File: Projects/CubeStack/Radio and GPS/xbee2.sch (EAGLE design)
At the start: 78 parts, among them Q1 310mA/60V/1.6Ω, Q2 310mA/60V/1.6Ω, Q3 310mA/60V/1.6Ω, Q4 310mA/60V/1.6Ω, U1 TS3USB221A, U2 SPARKFUN-IC-POWER_V_REG_MIC52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, U3 TS3USB221A, U4 SPARKFUN-IC-POWER_V_REG_MIC52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, U5 Value, U6 CPSS_IC_TPS62130_RGT_16

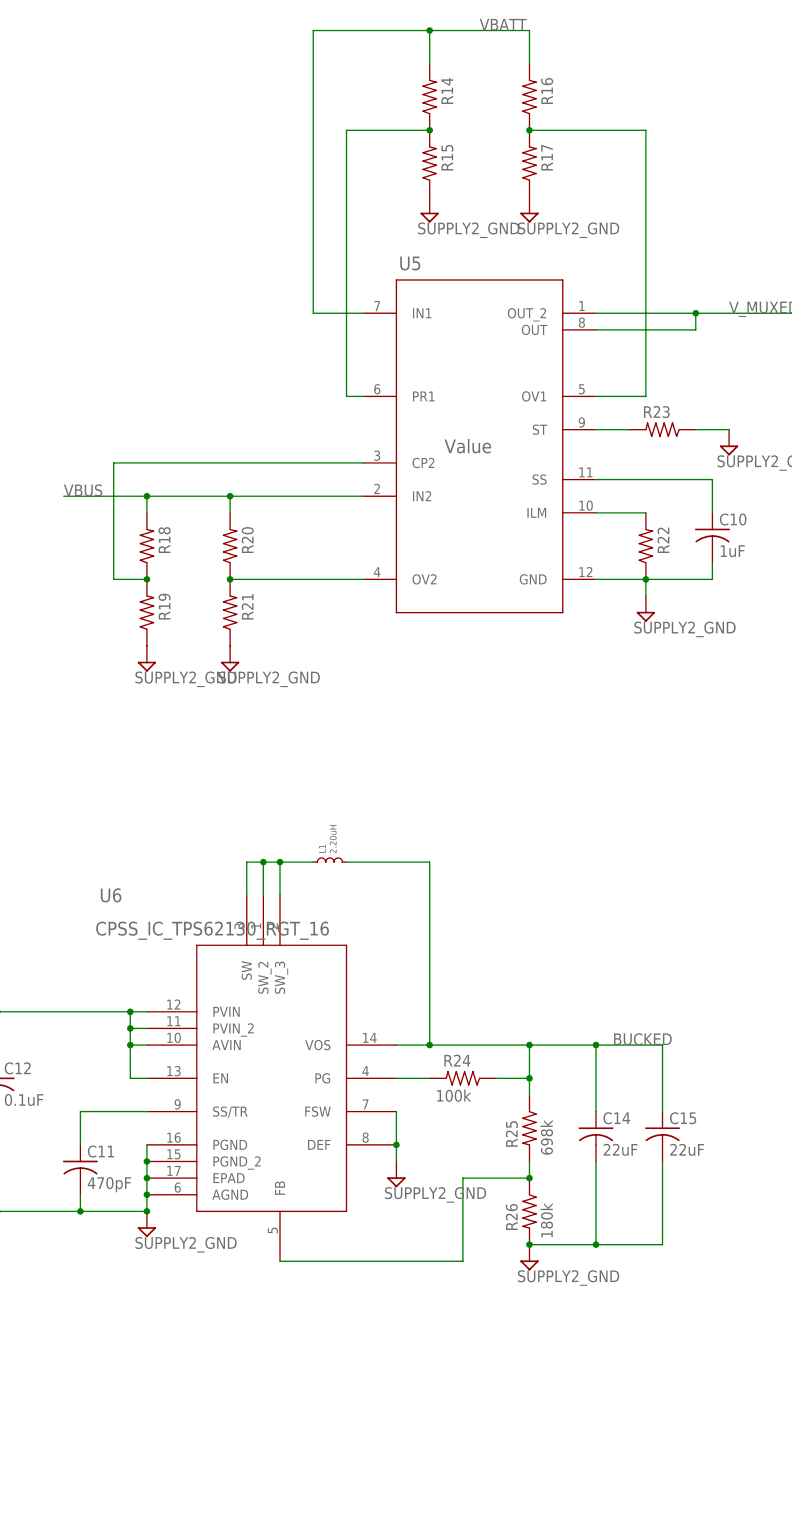
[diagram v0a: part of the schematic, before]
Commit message: Added some part values
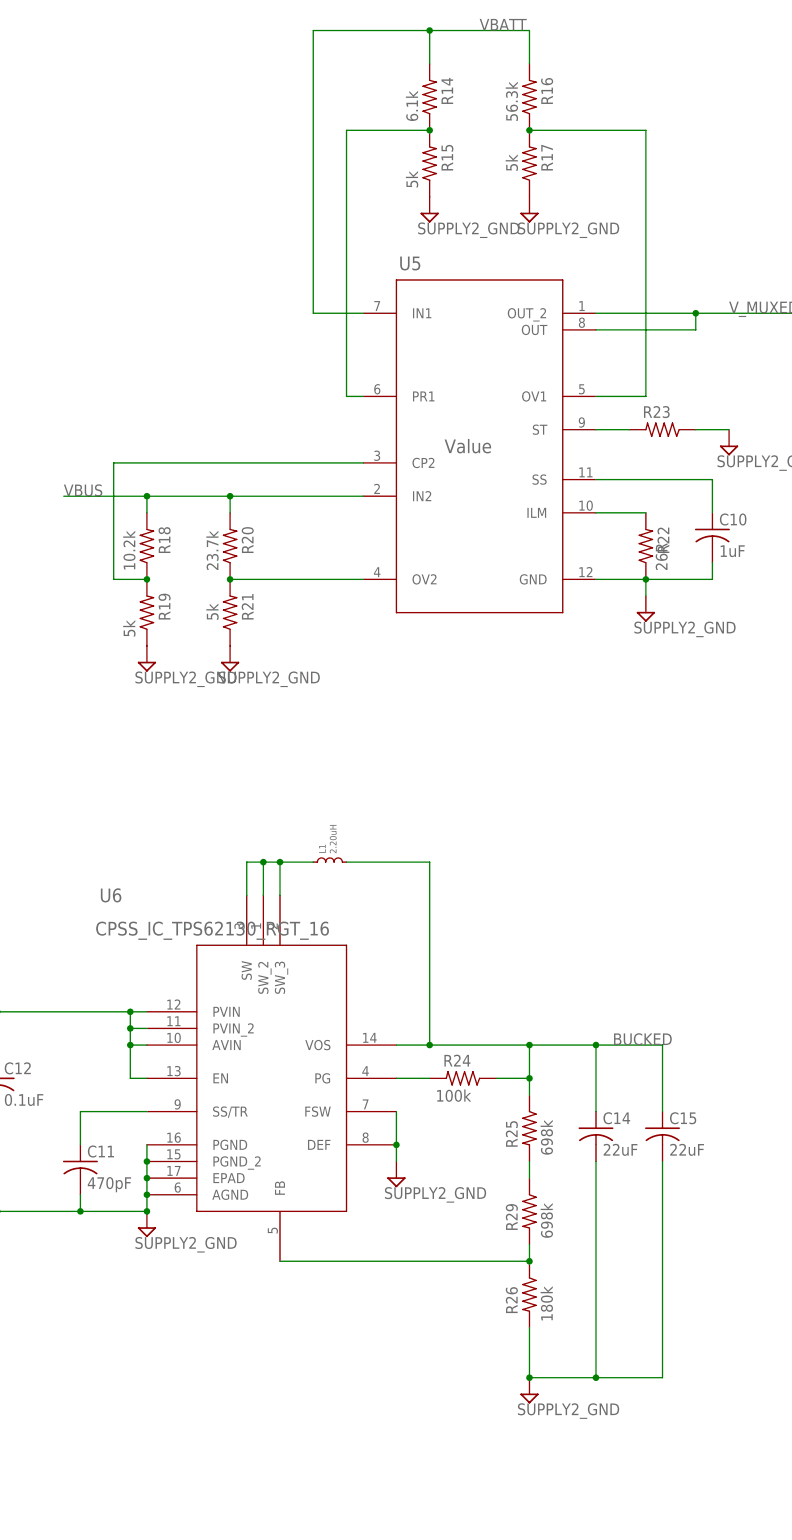
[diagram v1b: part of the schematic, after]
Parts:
- added R29: 698k, xbee2:RESISTOR_R-US_R0402
- R14: value (none) -> 6.1k
- R15, R17, R19, R21: value (none) -> 5k
- R16: value (none) -> 56.3k
- R18: value (none) -> 10.2k
- R20: value (none) -> 23.7k
- R22: value (none) -> 26R
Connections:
- new net N$40: R25.2, R29.1
- net N$24: now also R29.2; no longer R25.2
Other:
- moved on the sheet: R26
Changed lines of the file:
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@@
 <drawing>
 <settings>
-<setting alwaysvectorfont="no"/>
+<setting alwaysvectorfont="yes"/>
 <setting verticaltext="up"/>
 </settings>
@@
 <part name="R13" library="xbee2" deviceset="RESISTOR_R-US_" device="R0402" value="10k"/>
 <part name="U5" library="xbee2" deviceset="CPSS_IC_TPS2121RUXR" device="" value="Value"/>
-<part name="R14" library="xbee2" deviceset="RESISTOR_R-US_" device="R0402"/>
-<part name="R15" library="xbee2" deviceset="RESISTOR_R-US_" device="R0402"/>
+<part name="R14" library="xbee2" deviceset="RESISTOR_R-US_" device="R0402" value="6.1k"/>
+<part name="R15" library="xbee2" deviceset="RESISTOR_R-US_" device="R0402" value="5k"/>
 <part name="SUPPLY12" library="xbee2" deviceset="SUPPLY2_GND" device=""/>
-<part name="R16" library="xbee2" deviceset="RESISTOR_R-US_" device="R0402"/>
-<part name="R17" library="xbee2" deviceset="RESISTOR_R-US_" device="R0402"/>
+<part name="R16" library="xbee2" deviceset="RESISTOR_R-US_" device="R0402" value="56.3k"/>
+<part name="R17" library="xbee2" deviceset="RESISTOR_R-US_" device="R0402" value="5k"/>
 <part name="SUPPLY13" library="xbee2" deviceset="SUPPLY2_GND" device=""/>
-<part name="R18" library="xbee2" deviceset="RESISTOR_R-US_" device="R0402"/>
-<part name="R19" library="xbee2" deviceset="RESISTOR_R-US_" device="R0402"/>
+<part name="R18" library="xbee2" deviceset="RESISTOR_R-US_" device="R0402" value="10.2k"/>
+<part name="R19" library="xbee2" deviceset="RESISTOR_R-US_" device="R0402" value="5k"/>
 <part name="SUPPLY14" library="xbee2" deviceset="SUPPLY2_GND" device=""/>
-<part name="R20" library="xbee2" deviceset="RESISTOR_R-US_" device="R0402"/>
-<part name="R21" library="xbee2" deviceset="RESISTOR_R-US_" device="R0402"/>
+<part name="R20" library="xbee2" deviceset="RESISTOR_R-US_" device="R0402" value="23.7k"/>
+<part name="R21" library="xbee2" deviceset="RESISTOR_R-US_" device="R0402" value="5k"/>
 <part name="SUPPLY15" library="xbee2" deviceset="SUPPLY2_GND" device=""/>
-<part name="R22" library="xbee2" deviceset="RESISTOR_R-US_" device="R0402"/>
+<part name="R22" library="xbee2" deviceset="RESISTOR_R-US_" device="R0402" value="26R"/>
 <part name="C10" library="xbee2" deviceset="RESISTOR_C-US" device="C0402" value="1uF"/>
 <part name="SUPPLY16" library="xbee2" deviceset="SUPPLY2_GND" device=""/>
@@
 <part name="SJ7" library="xbee2" deviceset="JUMPER_SJ2W" device=""/>
 <part name="SJ8" library="xbee2" deviceset="JUMPER_SJ2W" device=""/>
+<part name="R29" library="xbee2" deviceset="RESISTOR_R-US_" device="R0402" value="698k"/>
 </parts>
 <sheets>
@@
 <instance part="R14" gate="G$1" x="-60.96" y="312.42" smashed="yes" rot="R90">
 <attribute name="NAME" x="-57.3786" y="311.15" size="1.778" layer="95" rot="R90"/>
-<attribute name="VALUE" x="-57.658" y="308.61" size="1.778" layer="96" rot="R90"/>
+<attribute name="VALUE" x="-62.738" y="308.61" size="1.778" layer="96" rot="R90"/>
 </instance>
 <instance part="R15" gate="G$1" x="-60.96" y="302.26" smashed="yes" rot="R90">
 <attribute name="NAME" x="-57.3786" y="300.99" size="1.778" layer="95" rot="R90"/>
-<attribute name="VALUE" x="-57.658" y="298.45" size="1.778" layer="96" rot="R90"/>
+<attribute name="VALUE" x="-62.738" y="298.45" size="1.778" layer="96" rot="R90"/>
 </instance>
 <instance part="SUPPLY12" gate="GND" x="-60.96" y="294.64" smashed="yes">
@@
 <instance part="R16" gate="G$1" x="-45.72" y="312.42" smashed="yes" rot="R90">
 <attribute name="NAME" x="-42.1386" y="311.15" size="1.778" layer="95" rot="R90"/>
-<attribute name="VALUE" x="-42.418" y="308.61" size="1.778" layer="96" rot="R90"/>
+<attribute name="VALUE" x="-47.498" y="308.61" size="1.778" layer="96" rot="R90"/>
 </instance>
 <instance part="R17" gate="G$1" x="-45.72" y="302.26" smashed="yes" rot="R90">
 <attribute name="NAME" x="-42.1386" y="300.99" size="1.778" layer="95" rot="R90"/>
-<attribute name="VALUE" x="-42.418" y="298.45" size="1.778" layer="96" rot="R90"/>
+<attribute name="VALUE" x="-47.498" y="300.99" size="1.778" layer="96" rot="R90"/>
 </instance>
 <instance part="SUPPLY13" gate="GND" x="-45.72" y="294.64" smashed="yes">
@@
 <instance part="R18" gate="G$1" x="-104.14" y="243.84" smashed="yes" rot="R90">
 <attribute name="NAME" x="-100.5586" y="242.57" size="1.778" layer="95" rot="R90"/>
-<attribute name="VALUE" x="-100.838" y="240.03" size="1.778" layer="96" rot="R90"/>
+<attribute name="VALUE" x="-105.918" y="240.03" size="1.778" layer="96" rot="R90"/>
 </instance>
 <instance part="R19" gate="G$1" x="-104.14" y="233.68" smashed="yes" rot="R90">
 <attribute name="NAME" x="-100.5586" y="232.41" size="1.778" layer="95" rot="R90"/>
-<attribute name="VALUE" x="-100.838" y="229.87" size="1.778" layer="96" rot="R90"/>
+<attribute name="VALUE" x="-105.918" y="229.87" size="1.778" layer="96" rot="R90"/>
 </instance>
 <instance part="SUPPLY14" gate="GND" x="-104.14" y="226.06" smashed="yes">
@@
 <instance part="R20" gate="G$1" x="-91.44" y="243.84" smashed="yes" rot="R90">
 <attribute name="NAME" x="-87.8586" y="242.57" size="1.778" layer="95" rot="R90"/>
-<attribute name="VALUE" x="-88.138" y="240.03" size="1.778" layer="96" rot="R90"/>
+<attribute name="VALUE" x="-93.218" y="240.03" size="1.778" layer="96" rot="R90"/>
 </instance>
 <instance part="R21" gate="G$1" x="-91.44" y="233.68" smashed="yes" rot="R90">
 <attribute name="NAME" x="-87.8586" y="232.41" size="1.778" layer="95" rot="R90"/>
-<attribute name="VALUE" x="-88.138" y="229.87" size="1.778" layer="96" rot="R90"/>
+<attribute name="VALUE" x="-93.218" y="232.41" size="1.778" layer="96" rot="R90"/>
 </instance>
 <instance part="SUPPLY15" gate="GND" x="-91.44" y="226.06" smashed="yes">
@@
 <attribute name="VALUE" x="-43.942" y="156.21" size="1.778" layer="96" rot="R270"/>
 </instance>
-<instance part="R26" gate="G$1" x="-45.72" y="142.24" smashed="yes" rot="R270">
-<attribute name="NAME" x="-49.3014" y="143.51" size="1.778" layer="95" rot="R270"/>
-<attribute name="VALUE" x="-43.942" y="143.51" size="1.778" layer="96" rot="R270"/>
-</instance>
-<instance part="SUPPLY20" gate="GND" x="-45.72" y="134.62" smashed="yes">
-<attribute name="VALUE" x="-47.625" y="131.445" size="1.778" layer="96"/>
+<instance part="R26" gate="G$1" x="-45.72" y="129.54" smashed="yes" rot="R270">
+<attribute name="NAME" x="-49.3014" y="130.81" size="1.778" layer="95" rot="R270"/>
+<attribute name="VALUE" x="-43.942" y="130.81" size="1.778" layer="96" rot="R270"/>
+</instance>
+<instance part="SUPPLY20" gate="GND" x="-45.72" y="114.3" smashed="yes">
+<attribute name="VALUE" x="-47.625" y="111.125" size="1.778" layer="96"/>
 </instance>
 <instance part="L1" gate="G$1" x="-76.2" y="195.58" smashed="yes">
@@
 <attribute name="NAME" x="198.12" y="-63.119" size="1.778" layer="95"/>
 <attribute name="VALUE" x="198.12" y="-65.405" size="1.778" layer="96"/>
+</instance>
+<instance part="R29" gate="G$1" x="-45.72" y="142.24" smashed="yes" rot="R270">
+<attribute name="NAME" x="-49.3014" y="143.51" size="1.778" layer="95" rot="R270"/>
+<attribute name="VALUE" x="-43.942" y="143.51" size="1.778" layer="96" rot="R270"/>
 </instance>
 </instances>
@@
 <pinref part="SUPPLY20" gate="GND" pin="GND"/>
 <pinref part="C14" gate="G$1" pin="2"/>
-<wire x1="-35.56" y1="149.86" x2="-35.56" y2="137.16" width="0.1524" layer="91"/>
-<wire x1="-35.56" y1="137.16" x2="-45.72" y2="137.16" width="0.1524" layer="91"/>
-<junction x="-45.72" y="137.16"/>
+<wire x1="-35.56" y1="149.86" x2="-35.56" y2="116.84" width="0.1524" layer="91"/>
+<wire x1="-35.56" y1="116.84" x2="-45.72" y2="116.84" width="0.1524" layer="91"/>
+<junction x="-45.72" y="116.84"/>
 <pinref part="C15" gate="G$1" pin="2"/>
-<wire x1="-25.4" y1="149.86" x2="-25.4" y2="137.16" width="0.1524" layer="91"/>
-<wire x1="-25.4" y1="137.16" x2="-35.56" y2="137.16" width="0.1524" layer="91"/>
-<junction x="-35.56" y="137.16"/>
+<wire x1="-25.4" y1="149.86" x2="-25.4" y2="116.84" width="0.1524" layer="91"/>
+<wire x1="-25.4" y1="116.84" x2="-35.56" y2="116.84" width="0.1524" layer="91"/>
+<junction x="-35.56" y="116.84"/>
+<wire x1="-45.72" y1="116.84" x2="-45.72" y2="124.46" width="0.1524" layer="91"/>
 </segment>
 <segment>
@@
 <net name="N$24" class="0">
 <segment>
-<pinref part="R25" gate="G$1" pin="2"/>
 <pinref part="R26" gate="G$1" pin="1"/>
-<wire x1="-45.72" y1="149.86" x2="-45.72" y2="147.32" width="0.1524" layer="91"/>
 <pinref part="U6" gate="A" pin="FB"/>
-<wire x1="-83.82" y1="134.62" x2="-55.88" y2="134.62" width="0.1524" layer="91"/>
-<wire x1="-55.88" y1="134.62" x2="-55.88" y2="147.32" width="0.1524" layer="91"/>
-<wire x1="-55.88" y1="147.32" x2="-45.72" y2="147.32" width="0.1524" layer="91"/>
-<junction x="-45.72" y="147.32"/>
+<wire x1="-83.82" y1="134.62" x2="-45.72" y2="134.62" width="0.1524" layer="91"/>
+<pinref part="R29" gate="G$1" pin="2"/>
+<wire x1="-45.72" y1="134.62" x2="-45.72" y2="137.16" width="0.1524" layer="91"/>
+<junction x="-45.72" y="134.62"/>
 </segment>
 </net>
@@
 </segment>
 </net>
+<net name="N$40" class="0">
+<segment>
+<pinref part="R29" gate="G$1" pin="1"/>
+<pinref part="R25" gate="G$1" pin="2"/>
+<wire x1="-45.72" y1="147.32" x2="-45.72" y2="149.86" width="0.1524" layer="91"/>
+</segment>
+</net>
